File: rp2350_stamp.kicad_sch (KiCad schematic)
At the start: 42 parts, among them J1 Conn_West, J2 Conn_North, J3 Conn_South, J4 Conn_East, Q1 BSS84, SW1 SW_RESET, SW2 SW_BOOTSEL, U1 W25Q128JVPIQ, U2 XT4051, U3 AP2112K-3.3, U4 RP235x-A, Y1 XYDBPCNANF-12MHZ

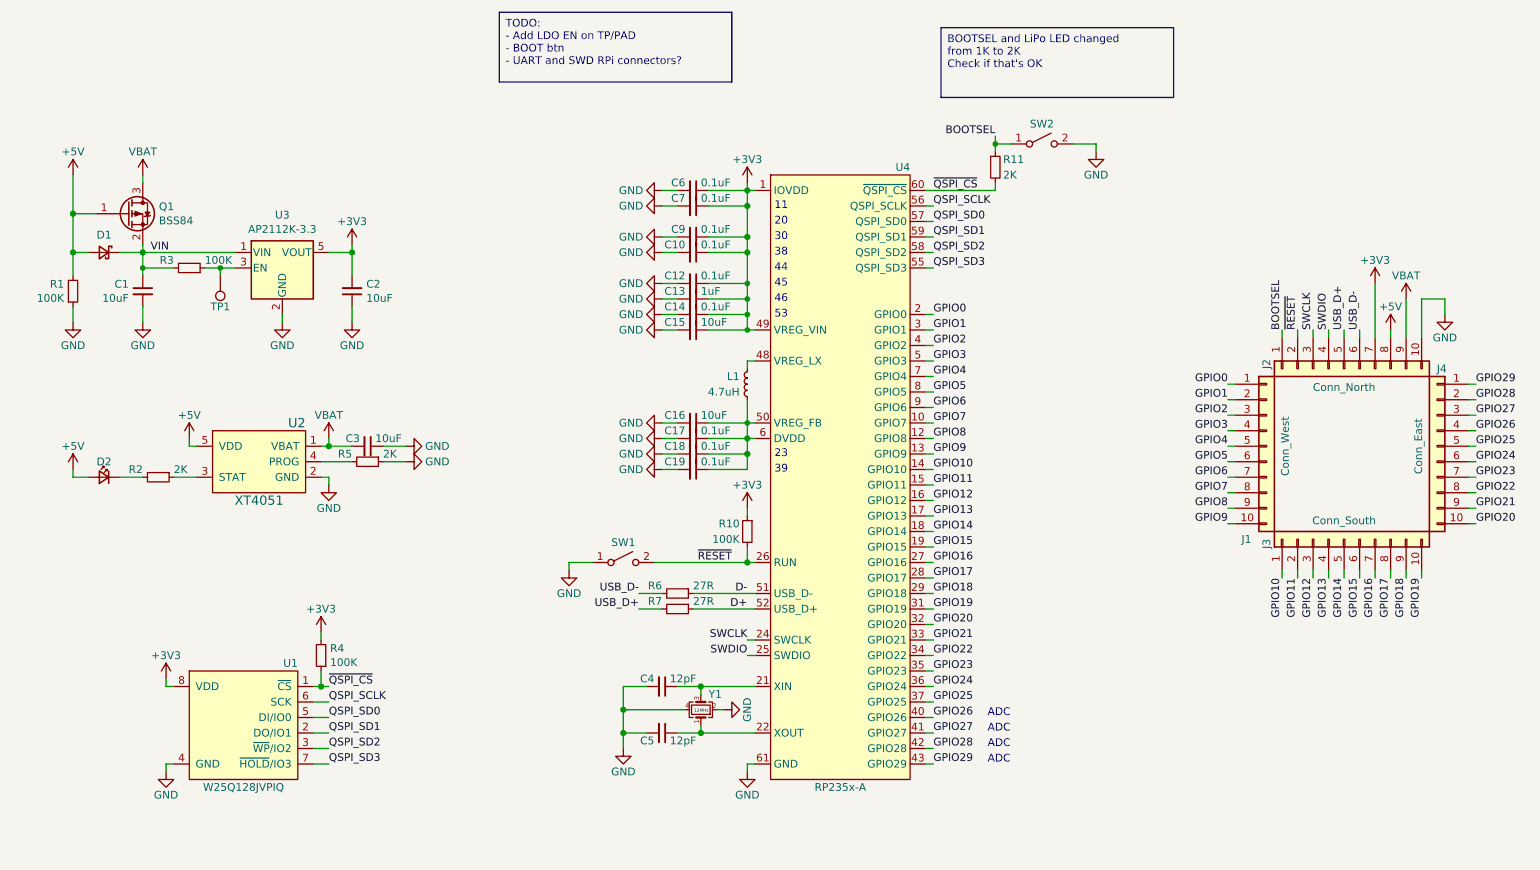
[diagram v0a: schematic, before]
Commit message: Rev 2
Swapped back to SOT-23 LiPo charger
Added QR Code
Added LDO EN back silk
Moved around front silk
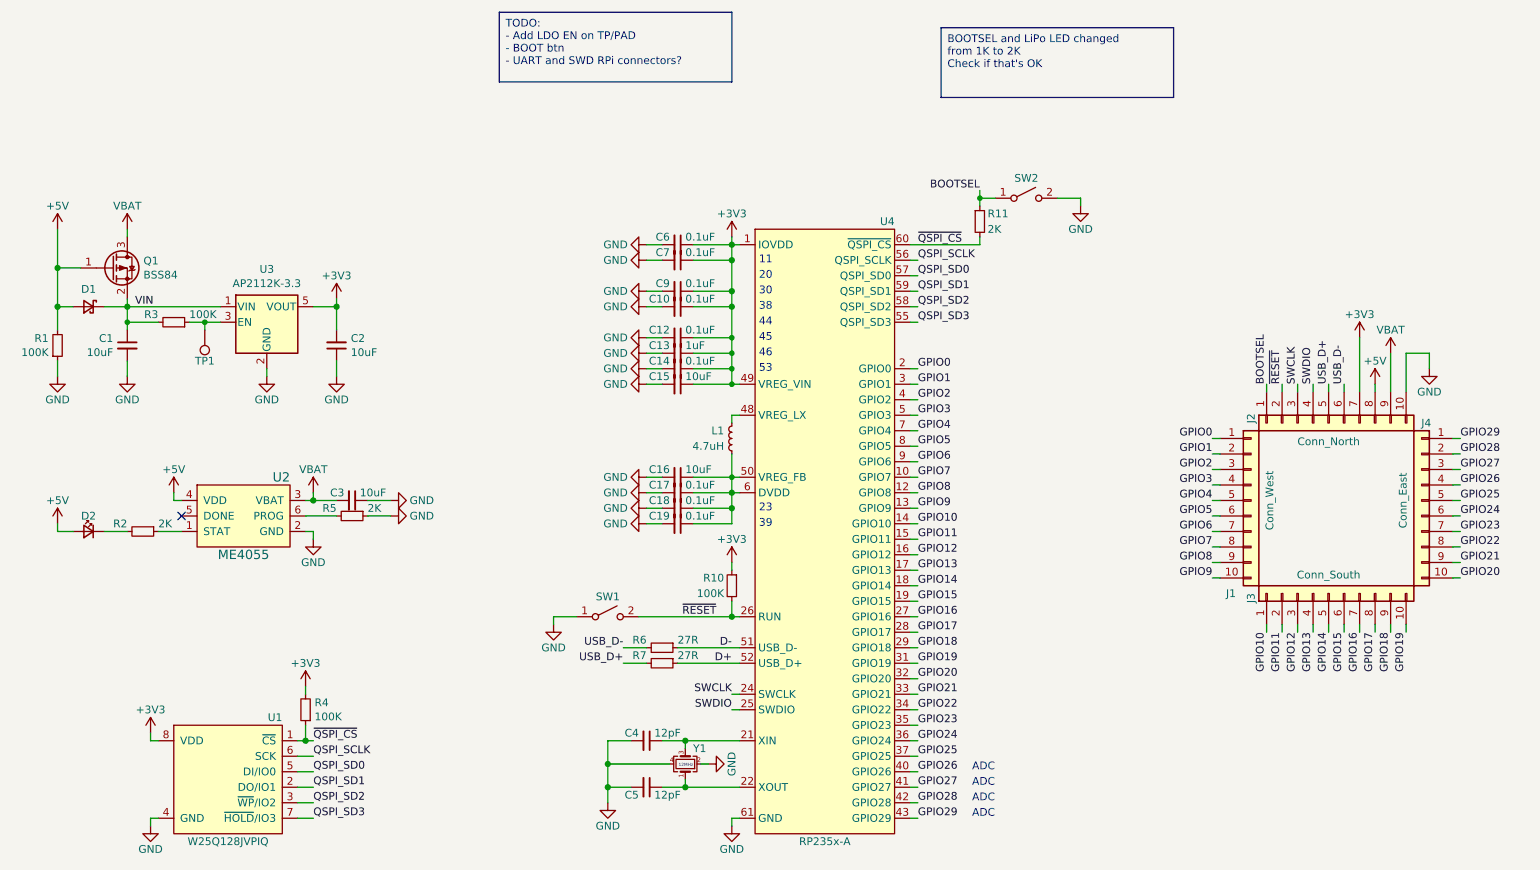
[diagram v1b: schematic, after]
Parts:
- U2: value XT4051 -> ME4055; footprint Package_TO_SOT_SMD:SOT-553 -> Package_TO_SOT_SMD:SOT-23-6; symbol Battery_Management_Extra: XT4051 -> Battery_Management_Extra:ME4055-N; LCSC C219186 -> C82121
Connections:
- net +5V: now also U2.4 (VDD); no longer U2.5 (VDD)
- net VBAT: now also U2.3 (VBAT); no longer U2.1 (VBAT)
- net at R2.1: now also U2.1 (STAT); no longer U2.3 (STAT)
- net at R5.2: now also U2.6 (PROG); no longer U2.4 (PROG)
- no-connect marks 0 -> 1
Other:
- title: (none) -> RP2350 Stamp
- moved on the sheet: C1, C10, C12, C13, C14, C15, C16, C17, C18, C19, C2, C3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

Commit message: Rev 3
Added a solder jumper for BAT LED
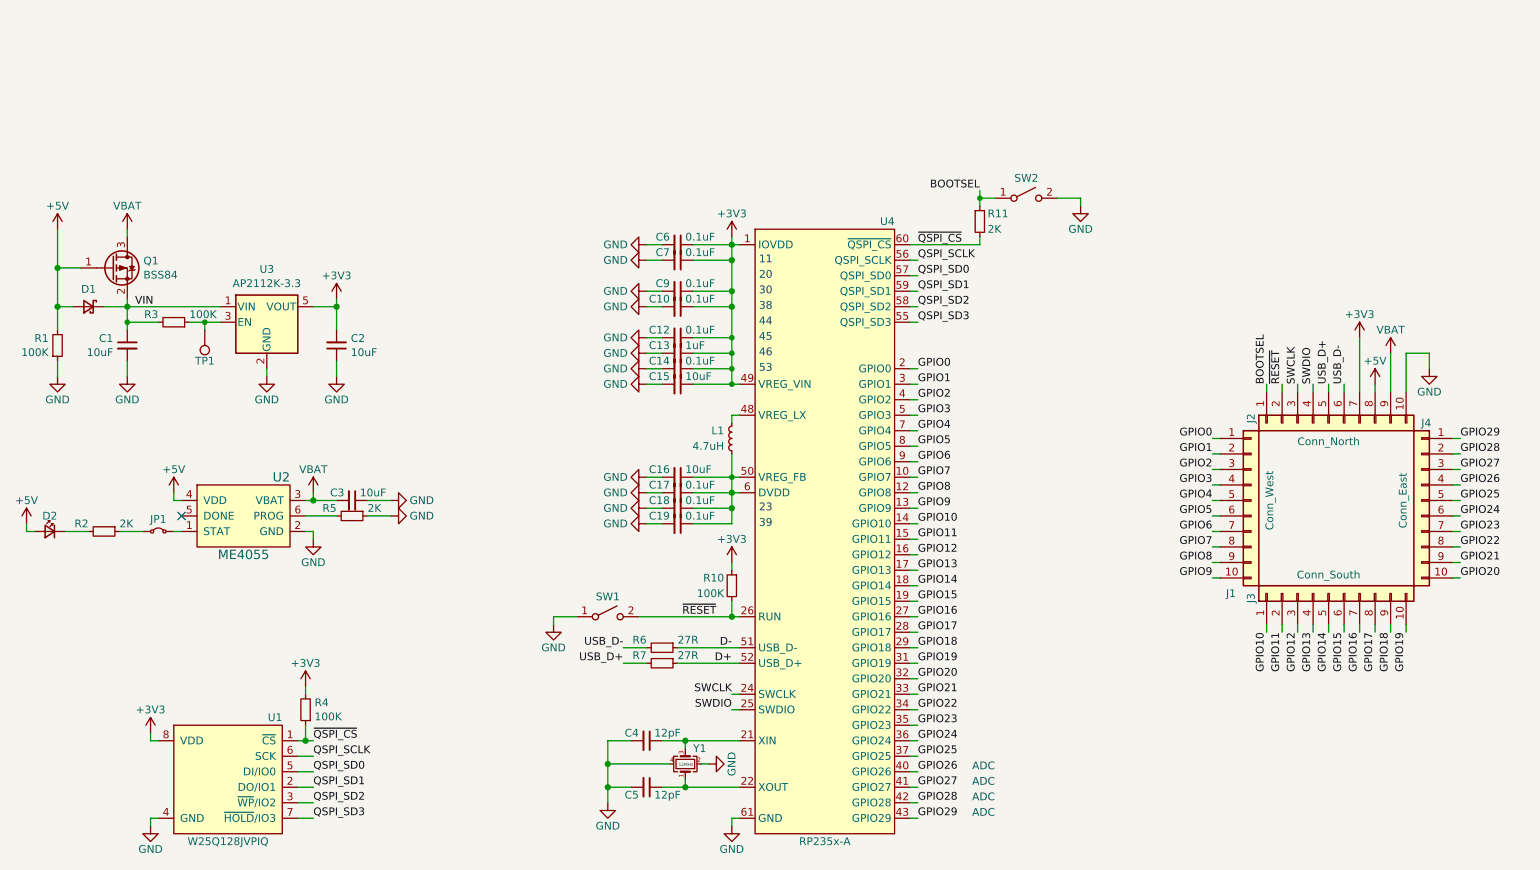
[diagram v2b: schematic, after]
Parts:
- added JP1: SJ_STAT_LED, Jumper:SolderJumper-2_P1.3mm_Bridged_RoundedPad1.0x1.5mm, symbol Jumper:Jumper_2_Small_Bridged
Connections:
- net at U2.1 (STAT): now also JP1.2 (B); no longer R2.1
- new net: JP1.1 (A), R2.1
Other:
- moved on the sheet: D2, R2
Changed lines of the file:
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@@
 	(wire
 		(pts
+			(xy 26.67 105.41) (xy 27.94 105.41)
+		)
+		(stroke
+			(width 0)
+			(type default)
+		)
+	)
+	(wire
+		(pts
 			(xy 171.45 68.58) (xy 172.72 68.58)
 		)
@@
 	(wire
 		(pts
-			(xy 31.75 105.41) (xy 31.75 104.14)
+			(xy 26.67 105.41) (xy 26.67 104.14)
 		)
 		(stroke
@@
 	(wire
 		(pts
-			(xy 52.07 105.41) (xy 48.26 105.41)
+			(xy 52.07 105.41) (xy 50.8 105.41)
 		)
 		(stroke
@@
 	(wire
 		(pts
-			(xy 43.18 105.41) (xy 39.37 105.41)
+			(xy 36.83 105.41) (xy 33.02 105.41)
 		)
 		(stroke
@@
 	(wire
 		(pts
+			(xy 41.91 105.41) (xy 45.72 105.41)
+		)
+		(stroke
+			(width 0)
+			(type default)
+		)
+	)
+	(wire
+		(pts
 			(xy 71.12 147.32) (xy 73.66 147.32)
 		)
@@
 	(wire
 		(pts
-			(xy 31.75 105.41) (xy 34.29 105.41)
-		)
-		(stroke
-			(width 0)
-			(type solid)
-		)
-	)
-	(wire
-		(pts
 			(xy 171.45 83.82) (xy 172.72 83.82)
 		)
@@
 		)
 	)
-	(text_box "BOOTSEL and LiPo LED changed from 1K to 2K\nCheck if that's OK"
-		(exclude_from_sim no)
-		(at 176.53 22.86 0)
-		(size 38.1 11.43)
-		(stroke
-			(width 0)
-			(type default)
-		)
-		(fill
-			(type none)
-		)
-		(effects
-			(font
-				(size 1.27 1.27)
-			)
-			(justify left top)
-		)
-	)
-	(text_box "TODO:\n- Add LDO EN on TP/PAD\n- BOOT btn\n- UART and SWD RPi connectors?"
-		(exclude_from_sim no)
-		(at 104.14 20.32 0)
-		(size 38.1 11.43)
-		(stroke
-			(width 0)
-			(type default)
-		)
-		(fill
-			(type none)
-		)
-		(effects
-			(font
-				(size 1.27 1.27)
-			)
-			(justify left top)
-		)
-	)
 	(text "53"
 		(exclude_from_sim no)
@@
 	(symbol
 		(lib_id "power:+5V")
-		(at 31.75 104.14 0)
+		(at 26.67 104.14 0)
 		(unit 1)
 		(exclude_from_sim no)
@@
 		(dnp no)
 		(property "Reference" "#PWR03"
-			(at 31.75 107.95 0)
+			(at 26.67 107.95 0)
 			(effects
 				(font
@@
 		)
 		(property "Value" "+5V"
-			(at 31.75 100.33 0)
+			(at 26.67 100.33 0)
 			(effects
 				(font
@@
 		)
 		(property "Footprint" ""
-			(at 31.75 104.14 0)
+			(at 26.67 104.14 0)
 			(effects
 				(font
@@
 		)
 		(property "Datasheet" ""
-			(at 31.75 104.14 0)
+			(at 26.67 104.14 0)
 			(effects
 				(font
@@
 		)
 		(property "Description" ""
-			(at 31.75 104.14 0)
+			(at 26.67 104.14 0)
 			(effects
 				(font
@@
 	)
 	(symbol
+		(lib_id "Jumper:Jumper_2_Small_Bridged")
+		(at 48.26 105.41 0)
+		(unit 1)
+		(exclude_from_sim yes)
+		(in_bom no)
+		(on_board yes)
+		(dnp no)
+		(property "Reference" "JP1"
+			(at 48.26 104.14 0)
+			(effects
+				(font
+					(size 1.27 1.27)
+				)
+				(justify bottom)
+			)
+		)
+		(property "Value" "SJ_STAT_LED"
+			(at 48.26 106.68 0)
+			(effects
+				(font
+					(size 1.27 1.27)
+				)
+				(justify top)
+				(hide yes)
+			)
+		)
+		(property "Footprint" "Jumper:SolderJumper-2_P1.3mm_Bridged_RoundedPad1.0x1.5mm"
+			(at 48.26 105.41 0)
+			(effects
+				(font
+					(size 1.27 1.27)
+				)
+				(hide yes)
+			)
+		)
+		(property "Datasheet" "~"
+			(at 48.26 105.41 0)
+			(effects
+				(font
+					(size 1.27 1.27)
+				)
+				(hide yes)
+			)
+		)
+		(property "Description" "Jumper, 2-pole, small symbol, bridged"
+			(at 48.26 105.41 0)
+			(effects
+				(font
+					(size 1.27 1.27)
+				)
+				(hide yes)
+			)
+		)
+		(pin "1"
+		)
+		(pin "2"
+		)
+		(instances
+			(project "rp2350_stamp"
+				(path "/019f2816-6bfb-4531-95b3-45f73cf5fc4b"
+					(reference "JP1")
+					(unit 1)
+				)
+			)
+		)
+	)
+	(symbol
 		(lib_id "power:GND")
 		(at 43.18 80.01 0)
@@
 	(symbol
 		(lib_id "Device:R_Small")
-		(at 45.72 105.41 270)
+		(at 39.37 105.41 270)
 		(unit 1)
 		(exclude_from_sim no)
@@
 		(dnp no)
 		(property "Reference" "R2"
-			(at 43.18 104.14 90)
+			(at 36.83 104.14 90)
 			(effects
 				(font
@@
 		)
 		(property "Value" "2K"
-			(at 48.26 104.14 90)
+			(at 41.91 104.14 90)
 			(effects
 				(font
@@
 		)
 		(property "Footprint" "Resistor_SMD:R_0603_1608Metric"
-			(at 45.72 105.41 0)
+			(at 39.37 105.41 0)
 			(effects
 				(font
@@
 		)
 		(property "Datasheet" "~"
-			(at 45.72 105.41 0)
+			(at 39.37 105.41 0)
 			(effects
 				(font
@@
 		)
 		(property "Description" ""
-			(at 45.72 105.41 0)
+			(at 39.37 105.41 0)
 			(effects
 				(font
@@
 	(symbol
 		(lib_id "Device:LED_Small")
-		(at 36.83 105.41 0)
+		(at 30.48 105.41 0)
 		(mirror y)
 		(unit 1)
@@
 		(dnp no)
 		(property "Reference" "D2"
-			(at 36.83 102.87 0)
+			(at 30.48 102.87 0)
 			(effects
 				(font
@@
 		)
 		(property "Value" "LED_CHR"
-			(at 36.83 101.7524 0)
+			(at 30.48 101.7524 0)
 			(effects
 				(font
@@
 		)
 		(property "Footprint" "LED_SMD:LED_0603_1608Metric"
-			(at 36.83 105.41 90)
+			(at 30.48 105.41 90)
 			(effects
 				(font
@@
 		)
 		(property "Datasheet" "~"
-			(at 36.83 105.41 90)
+			(at 30.48 105.41 90)
 			(effects
 				(font
@@
 		)
 		(property "Description" ""
-			(at 36.83 105.41 0)
+			(at 30.48 105.41 0)
 			(effects
 				(font
